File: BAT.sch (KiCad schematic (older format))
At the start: 4 parts

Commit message: assign vbat shunt footprint
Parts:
- R?: footprint 3920 -> ottojo_resistor:R_3920
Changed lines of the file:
@@
 F 0 "R?" V 2800 3000 50  0000 C CNN
 F 1 "2m" V 2900 3000 50  0000 C CNN
-F 2 "3920" V 2730 3000 50  0001 C CNN
+F 2 "ottojo_resistor:R_3920" V 2730 3000 50  0001 C CNN
 F 3 "~" H 2800 3000 50  0001 C CNN
 F 4 ">=5.25W" V 2800 3000 50  0001 C CNN "Power"

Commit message: annotate parts
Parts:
- gave numbers to parts that had none: 4
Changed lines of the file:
@@
 P 2200 4150
 AR Path="/5C2CF18D/5C2F3706" Ref="#PWR?"  Part="1"
-AR Path="/5C2F335D/5C2F3706" Ref="#PWR?"  Part="1"
-F 0 "#PWR?" H 2200 3900 50  0001 C CNN
+AR Path="/5C2F335D/5C2F3706" Ref="#PWR020"  Part="1"
+F 0 "#PWR020" H 2200 3900 50  0001 C CNN
 F 1 "GND" V 2205 4022 50  0000 R CNN
 F 2 "" H 2200 4150 50  0001 C CNN
@@
 P 3550 3300
 AR Path="/5C2CF18D/5C2F3718" Ref="C?"  Part="1"
-AR Path="/5C2F335D/5C2F3718" Ref="C?"  Part="1"
-F 0 "C?" V 3650 3300 50  0000 C CNN
+AR Path="/5C2F335D/5C2F3718" Ref="C19"  Part="1"
+F 0 "C19" V 3650 3300 50  0000 C CNN
 F 1 "100n" V 3450 3300 50  0000 C CNN
 F 2 "Capacitor_SMD:C_0603_1608Metric" H 3550 3300 50  0001 C CNN
@@
 P 3700 3300
 AR Path="/5C2CF18D/5C2F3721" Ref="#PWR?"  Part="1"
-AR Path="/5C2F335D/5C2F3721" Ref="#PWR?"  Part="1"
-F 0 "#PWR?" H 3700 3050 50  0001 C CNN
+AR Path="/5C2F335D/5C2F3721" Ref="#PWR022"  Part="1"
+F 0 "#PWR022" H 3700 3050 50  0001 C CNN
 F 1 "GND" V 3705 3172 50  0000 R CNN
 F 2 "" H 3700 3300 50  0001 C CNN
@@
 P 2800 3000
 AR Path="/5C2CF18D/5C2F372C" Ref="R?"  Part="1"
-AR Path="/5C2F335D/5C2F372C" Ref="R?"  Part="1"
-F 0 "R?" V 2800 3000 50  0000 C CNN
+AR Path="/5C2F335D/5C2F372C" Ref="R17"  Part="1"
+F 0 "R17" V 2800 3000 50  0000 C CNN
 F 1 "2m" V 2900 3000 50  0000 C CNN
 F 2 "ottojo_resistor:R_3920" V 2730 3000 50  0001 C CNN
@@
 	4150 3000 4150 2900
 $Comp
-L amass:XT-F C?
+L amass:XT-F C20
 U 1 1 5C310632
 P 4450 3050
-F 0 "C?" H 4827 3101 50  0000 L CNN
+F 0 "C20" H 4827 3101 50  0000 L CNN
 F 1 "XT-F" H 4827 3010 50  0000 L CNN
 F 2 "XT60:XT60PW" H 4450 3050 50  0001 C CNN
@@
 	4300 3300 4300 3400
 $Comp
-L power:GND #PWR?
+L power:GND #PWR023
 U 1 1 5C3106E4
 P 4300 3400
-F 0 "#PWR?" H 4300 3150 50  0001 C CNN
+F 0 "#PWR023" H 4300 3150 50  0001 C CNN
 F 1 "GND" H 4305 3227 50  0000 C CNN
 F 2 "" H 4300 3400 50  0001 C CNN
@@
 P 2950 4850
 AR Path="/5C2CF18D/5C3168E6" Ref="#PWR?"  Part="1"
-AR Path="/5C2F335D/5C3168E6" Ref="#PWR?"  Part="1"
-F 0 "#PWR?" H 2950 4600 50  0001 C CNN
+AR Path="/5C2F335D/5C3168E6" Ref="#PWR021"  Part="1"
+F 0 "#PWR021" H 2950 4600 50  0001 C CNN
 F 1 "GND" V 2955 4722 50  0000 R CNN
 F 2 "" H 2950 4850 50  0001 C CNN
@@
 NoConn ~ 3600 4150
 $Comp
-L LTC2946:LTC2946 U?
+L LTC2946:LTC2946 U4
 U 1 1 5C32EA36
 P 2950 4050
-F 0 "U?" H 3450 3400 60  0000 C CNN
+F 0 "U4" H 3450 3400 60  0000 C CNN
 F 1 "LTC2946" H 2950 4050 60  0000 C CNN
 F 2 "Package_SO:MSOP-16_3x4mm_P0.5mm" H 3400 3200 60  0001 C CNN

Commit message: update XT60
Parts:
- C20: footprint XT60:XT60PW -> XT60:XT60PW-F
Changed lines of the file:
@@
 F 0 "C20" H 4827 3101 50  0000 L CNN
 F 1 "XT-F" H 4827 3010 50  0000 L CNN
-F 2 "XT60:XT60PW" H 4450 3050 50  0001 C CNN
+F 2 "XT60:XT60PW-F" H 4450 3050 50  0001 C CNN
 F 3 "" H 4450 3050 50  0001 C CNN
 	1    4450 3050

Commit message: wip und so
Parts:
- removed C20: XT-F, XT60:XT60PW-F, symbol amass:XT-F
- added J7: Conn_01x02_MountingPin, XT60:XT60PW-F, symbol Connector_Generic_MountingPin:Conn_01x02_MountingPin
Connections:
- wire segments 37 -> 33
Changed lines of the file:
@@
 EESchema Schematic File Version 4
 LIBS:PDB-cache
-EELAYER 26 0
+EELAYER 29 0
 EELAYER END
 $Descr A4 11693 8268
@@
 Wire Wire Line
 	4150 3000 4150 2900
-$Comp
-L amass:XT-F C20
-U 1 1 5C310632
-P 4450 3050
-F 0 "C20" H 4827 3101 50  0000 L CNN
-F 1 "XT-F" H 4827 3010 50  0000 L CNN
-F 2 "XT60:XT60PW-F" H 4450 3050 50  0001 C CNN
-F 3 "" H 4450 3050 50  0001 C CNN
-	1    4450 3050
-	1    0    0    -1
-$EndComp
-Wire Wire Line
-	4300 3100 4350 3100
 Wire Wire Line
 	4150 3000 4350 3000
-Wire Wire Line
-	4300 3100 4300 3200
-Wire Wire Line
-	4350 3200 4300 3200
-Connection ~ 4300 3200
-Wire Wire Line
-	4300 3200 4300 3300
-Wire Wire Line
-	4350 3300 4300 3300
-Connection ~ 4300 3300
 Text HLabel 4150 2900 1    50   Output ~ 0
 VBATOUT
@@
 	3000 3000 3050 3000
 Connection ~ 4150 3000
-Wire Wire Line
-	4300 3300 4300 3400
-$Comp
-L power:GND #PWR023
-U 1 1 5C3106E4
-P 4300 3400
-F 0 "#PWR023" H 4300 3150 50  0001 C CNN
-F 1 "GND" H 4305 3227 50  0000 C CNN
-F 2 "" H 4300 3400 50  0001 C CNN
-F 3 "" H 4300 3400 50  0001 C CNN
-	1    4300 3400
-	1    0    0    -1
-$EndComp
 Wire Wire Line
 	3050 3350 3050 3000
@@
 	1    0    0    -1
 $EndComp
+$Comp
+L Connector_Generic_MountingPin:Conn_01x02_MountingPin J7
+U 1 1 5CABAA0A
+P 4550 2900
+F 0 "J7" H 4638 2814 50  0000 L CNN
+F 1 "Conn_01x02_MountingPin" H 4638 2723 50  0000 L CNN
+F 2 "XT60:XT60PW-F" H 4550 2900 50  0001 C CNN
+F 3 "~" H 4550 2900 50  0001 C CNN
+	1    4550 2900
+	1    0    0    -1
+$EndComp
+Wire Wire Line
+	4350 2900 4300 2900
+Wire Wire Line
+	4300 2900 4300 2850
+$Comp
+L power:GND #PWR0103
+U 1 1 5CABC64B
+P 4300 2850
+F 0 "#PWR0103" H 4300 2600 50  0001 C CNN
+F 1 "GND" H 4305 2677 50  0000 C CNN
+F 2 "" H 4300 2850 50  0001 C CNN
+F 3 "" H 4300 2850 50  0001 C CNN
+	1    4300 2850
+	-1   0    0    1
+$EndComp
 $EndSCHEMATC

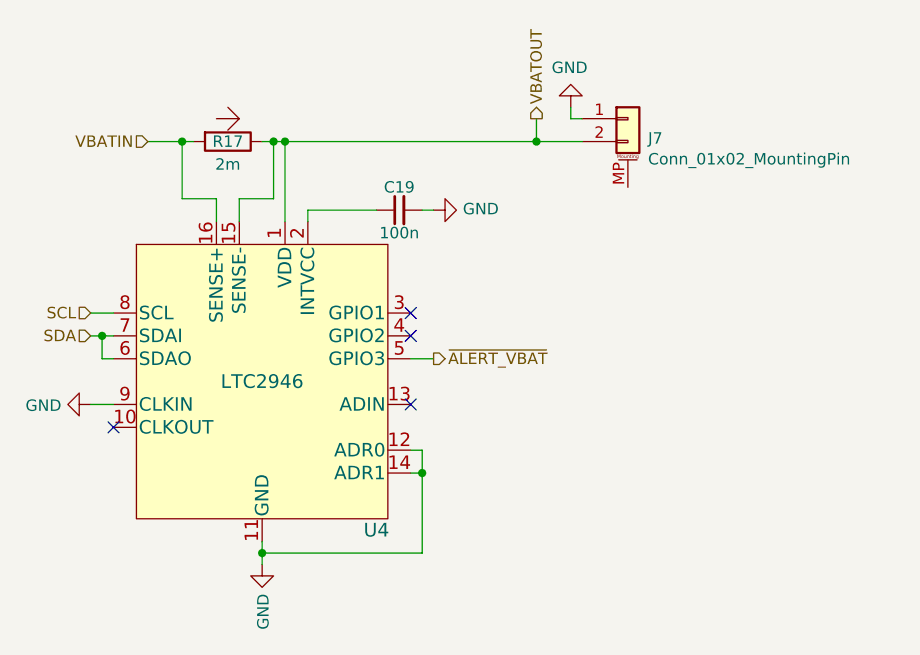
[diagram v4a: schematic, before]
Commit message: LMZM23600 from kicad libs
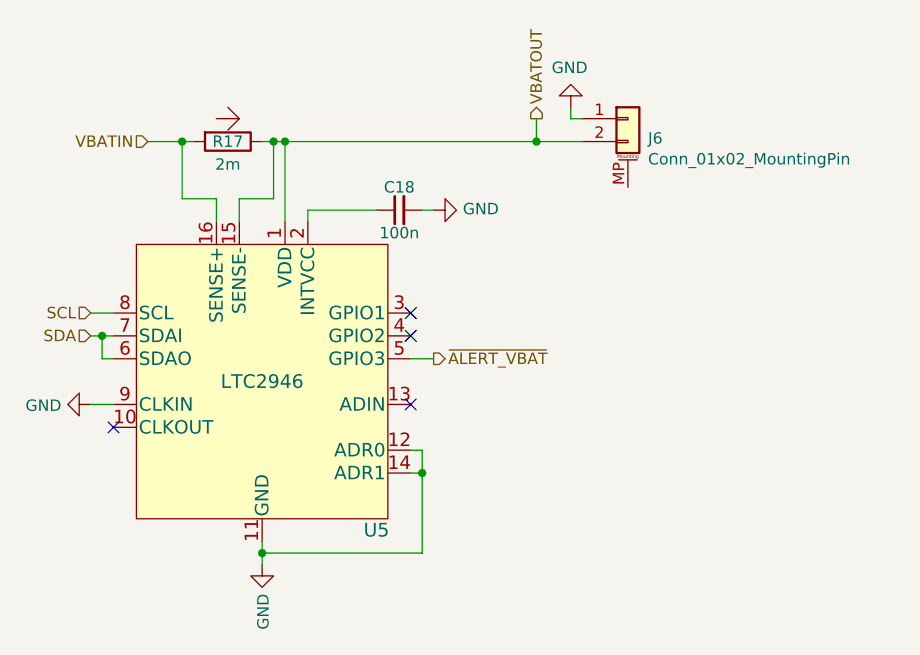
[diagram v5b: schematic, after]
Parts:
- renumbered C19 to C18, J7 to J6, U4 to U5
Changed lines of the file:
@@
 P 2200 4150
 AR Path="/5C2CF18D/5C2F3706" Ref="#PWR?"  Part="1"
-AR Path="/5C2F335D/5C2F3706" Ref="#PWR020"  Part="1"
-F 0 "#PWR020" H 2200 3900 50  0001 C CNN
+AR Path="/5C2F335D/5C2F3706" Ref="#PWR027"  Part="1"
+F 0 "#PWR027" H 2200 3900 50  0001 C CNN
 F 1 "GND" V 2205 4022 50  0000 R CNN
 F 2 "" H 2200 4150 50  0001 C CNN
@@
 P 3550 3300
 AR Path="/5C2CF18D/5C2F3718" Ref="C?"  Part="1"
-AR Path="/5C2F335D/5C2F3718" Ref="C19"  Part="1"
-F 0 "C19" V 3650 3300 50  0000 C CNN
+AR Path="/5C2F335D/5C2F3718" Ref="C18"  Part="1"
+F 0 "C18" V 3650 3300 50  0000 C CNN
 F 1 "100n" V 3450 3300 50  0000 C CNN
 F 2 "Capacitor_SMD:C_0603_1608Metric" H 3550 3300 50  0001 C CNN
@@
 P 3700 3300
 AR Path="/5C2CF18D/5C2F3721" Ref="#PWR?"  Part="1"
-AR Path="/5C2F335D/5C2F3721" Ref="#PWR022"  Part="1"
-F 0 "#PWR022" H 3700 3050 50  0001 C CNN
+AR Path="/5C2F335D/5C2F3721" Ref="#PWR029"  Part="1"
+F 0 "#PWR029" H 3700 3050 50  0001 C CNN
 F 1 "GND" V 3705 3172 50  0000 R CNN
 F 2 "" H 3700 3300 50  0001 C CNN
@@
 P 2950 4850
 AR Path="/5C2CF18D/5C3168E6" Ref="#PWR?"  Part="1"
-AR Path="/5C2F335D/5C3168E6" Ref="#PWR021"  Part="1"
-F 0 "#PWR021" H 2950 4600 50  0001 C CNN
+AR Path="/5C2F335D/5C3168E6" Ref="#PWR028"  Part="1"
+F 0 "#PWR028" H 2950 4600 50  0001 C CNN
 F 1 "GND" V 2955 4722 50  0000 R CNN
 F 2 "" H 2950 4850 50  0001 C CNN
@@
 NoConn ~ 3600 4150
 $Comp
-L LTC2946:LTC2946 U4
+L LTC2946:LTC2946 U5
 U 1 1 5C32EA36
 P 2950 4050
-F 0 "U4" H 3450 3400 60  0000 C CNN
+F 0 "U5" H 3450 3400 60  0000 C CNN
 F 1 "LTC2946" H 2950 4050 60  0000 C CNN
 F 2 "Package_SO:MSOP-16_3x4mm_P0.5mm" H 3400 3200 60  0001 C CNN
@@
 $EndComp
 $Comp
-L Connector_Generic_MountingPin:Conn_01x02_MountingPin J7
+L Connector_Generic_MountingPin:Conn_01x02_MountingPin J6
 U 1 1 5CABAA0A
 P 4550 2900
-F 0 "J7" H 4638 2814 50  0000 L CNN
+F 0 "J6" H 4638 2814 50  0000 L CNN
 F 1 "Conn_01x02_MountingPin" H 4638 2723 50  0000 L CNN
 F 2 "XT60:XT60PW-F" H 4550 2900 50  0001 C CNN
@@
 	4300 2900 4300 2850
 $Comp
-L power:GND #PWR0103
+L power:GND #PWR030
 U 1 1 5CABC64B
 P 4300 2850
-F 0 "#PWR0103" H 4300 2600 50  0001 C CNN
+F 0 "#PWR030" H 4300 2600 50  0001 C CNN
 F 1 "GND" H 4305 2677 50  0000 C CNN
 F 2 "" H 4300 2850 50  0001 C CNN

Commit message: more LEDs
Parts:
- renumbered R17 to R21
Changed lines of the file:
@@
 P 2800 3000
 AR Path="/5C2CF18D/5C2F372C" Ref="R?"  Part="1"
-AR Path="/5C2F335D/5C2F372C" Ref="R17"  Part="1"
-F 0 "R17" V 2800 3000 50  0000 C CNN
+AR Path="/5C2F335D/5C2F372C" Ref="R21"  Part="1"
+F 0 "R21" V 2800 3000 50  0000 C CNN
 F 1 "2m" V 2900 3000 50  0000 C CNN
 F 2 "ottojo_resistor:R_3920" V 2730 3000 50  0001 C CNN

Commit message: layout
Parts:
- renumbered J6 to J10
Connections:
- net GND: now also J10.MP (MountPin)
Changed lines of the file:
@@
 P 2200 4150
 AR Path="/5C2CF18D/5C2F3706" Ref="#PWR?"  Part="1"
-AR Path="/5C2F335D/5C2F3706" Ref="#PWR027"  Part="1"
-F 0 "#PWR027" H 2200 3900 50  0001 C CNN
+AR Path="/5C2F335D/5C2F3706" Ref="#PWR036"  Part="1"
+F 0 "#PWR036" H 2200 3900 50  0001 C CNN
 F 1 "GND" V 2205 4022 50  0000 R CNN
 F 2 "" H 2200 4150 50  0001 C CNN
@@
 P 3700 3300
 AR Path="/5C2CF18D/5C2F3721" Ref="#PWR?"  Part="1"
-AR Path="/5C2F335D/5C2F3721" Ref="#PWR029"  Part="1"
-F 0 "#PWR029" H 3700 3050 50  0001 C CNN
+AR Path="/5C2F335D/5C2F3721" Ref="#PWR038"  Part="1"
+F 0 "#PWR038" H 3700 3050 50  0001 C CNN
 F 1 "GND" V 3705 3172 50  0000 R CNN
 F 2 "" H 3700 3300 50  0001 C CNN
@@
 P 2950 4850
 AR Path="/5C2CF18D/5C3168E6" Ref="#PWR?"  Part="1"
-AR Path="/5C2F335D/5C3168E6" Ref="#PWR028"  Part="1"
-F 0 "#PWR028" H 2950 4600 50  0001 C CNN
+AR Path="/5C2F335D/5C3168E6" Ref="#PWR037"  Part="1"
+F 0 "#PWR037" H 2950 4600 50  0001 C CNN
 F 1 "GND" V 2955 4722 50  0000 R CNN
 F 2 "" H 2950 4850 50  0001 C CNN
@@
 	1    0    0    -1
 $EndComp
+Wire Wire Line
+	4350 2900 4300 2900
+Wire Wire Line
+	4300 2900 4300 2850
 $Comp
-L Connector_Generic_MountingPin:Conn_01x02_MountingPin J6
+L power:GND #PWR039
+U 1 1 5CABC64B
+P 4300 2850
+F 0 "#PWR039" H 4300 2600 50  0001 C CNN
+F 1 "GND" H 4305 2677 50  0000 C CNN
+F 2 "" H 4300 2850 50  0001 C CNN
+F 3 "" H 4300 2850 50  0001 C CNN
+	1    4300 2850
+	-1   0    0    1
+$EndComp
+$Comp
+L power:GND #PWR?
+U 1 1 5CAE44A2
+P 4550 3250
+F 0 "#PWR?" H 4550 3000 50  0001 C CNN
+F 1 "GND" H 4555 3077 50  0000 C CNN
+F 2 "" H 4550 3250 50  0001 C CNN
+F 3 "" H 4550 3250 50  0001 C CNN
+	1    4550 3250
+	1    0    0    -1
+$EndComp
+$Comp
+L Connector_Generic_MountingPin:Conn_01x02_MountingPin J10
 U 1 1 5CABAA0A
 P 4550 2900
-F 0 "J6" H 4638 2814 50  0000 L CNN
+F 0 "J10" H 4638 2814 50  0000 L CNN
 F 1 "Conn_01x02_MountingPin" H 4638 2723 50  0000 L CNN
 F 2 "XT60:XT60PW-F" H 4550 2900 50  0001 C CNN
@@
 $EndComp
 Wire Wire Line
-	4350 2900 4300 2900
-Wire Wire Line
-	4300 2900 4300 2850
-$Comp
-L power:GND #PWR030
-U 1 1 5CABC64B
-P 4300 2850
-F 0 "#PWR030" H 4300 2600 50  0001 C CNN
-F 1 "GND" H 4305 2677 50  0000 C CNN
-F 2 "" H 4300 2850 50  0001 C CNN
-F 3 "" H 4300 2850 50  0001 C CNN
-	1    4300 2850
-	-1   0    0    1
-$EndComp
+	4550 3200 4550 3250
 $EndSCHEMATC

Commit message: even more layout
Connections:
- net VBATOUT: no longer U5.1 (VDD)
- net 5VIN: now reaches C18.1, U5.2 (INTVCC)
- net 5VIN: now also U5.1 (VDD)
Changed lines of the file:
@@
 $Descr A4 11693 8268
 encoding utf-8
-Sheet 5 6
+Sheet 4 6
 Title "ToolboxPlane PDB: Battery Monitoring"
 Date "2019-01-03"
@@
 	3000 3250 3000 3000
 Connection ~ 3000 3000
-Wire Wire Line
-	3000 3000 3050 3000
 Connection ~ 4150 3000
-Wire Wire Line
-	3050 3350 3050 3000
-Connection ~ 3050 3000
-Wire Wire Line
-	3050 3000 4150 3000
 Wire Wire Line
 	3150 3350 3150 3300
@@
 NoConn ~ 3600 3750
 NoConn ~ 3600 4150
-$Comp
-L LTC2946:LTC2946 U5
-U 1 1 5C32EA36
-P 2950 4050
-F 0 "U5" H 3450 3400 60  0000 C CNN
-F 1 "LTC2946" H 2950 4050 60  0000 C CNN
-F 2 "Package_SO:MSOP-16_3x4mm_P0.5mm" H 3400 3200 60  0001 C CNN
-F 3 "https://www.analog.com/media/en/technical-documentation/data-sheets/2946fa.pdf" H 2950 4850 60  0001 C CNN
-	1    2950 4050
-	1    0    0    -1
-$EndComp
 Wire Wire Line
 	4350 2900 4300 2900
@@
 $EndComp
 $Comp
-L power:GND #PWR?
+L power:GND #PWR0108
 U 1 1 5CAE44A2
 P 4550 3250
-F 0 "#PWR?" H 4550 3000 50  0001 C CNN
+F 0 "#PWR0108" H 4550 3000 50  0001 C CNN
 F 1 "GND" H 4555 3077 50  0000 C CNN
 F 2 "" H 4550 3250 50  0001 C CNN
@@
 Wire Wire Line
 	4550 3200 4550 3250
+Wire Wire Line
+	3000 3000 4150 3000
+$Comp
+L LTC2946:LTC2946 U5
+U 1 1 5C32EA36
+P 2950 4050
+F 0 "U5" H 3450 3400 60  0000 C CNN
+F 1 "LTC2946" H 2950 4050 60  0000 C CNN
+F 2 "Package_SO:MSOP-16_3x4mm_P0.5mm" H 3400 3200 60  0001 C CNN
+F 3 "https://www.analog.com/media/en/technical-documentation/data-sheets/2946fa.pdf" H 2950 4850 60  0001 C CNN
+	1    2950 4050
+	1    0    0    -1
+$EndComp
+Wire Wire Line
+	3050 3350 3050 3300
+Wire Wire Line
+	3050 3300 3150 3300
+Connection ~ 3150 3300
+Wire Wire Line
+	3150 3300 3150 3100
+Wire Wire Line
+	3150 3100 3200 3100
+Text HLabel 3200 3100 2    50   Input ~ 0
+5VIN
 $EndSCHEMATC
